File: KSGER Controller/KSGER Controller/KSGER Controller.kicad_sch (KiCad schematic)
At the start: 49 parts

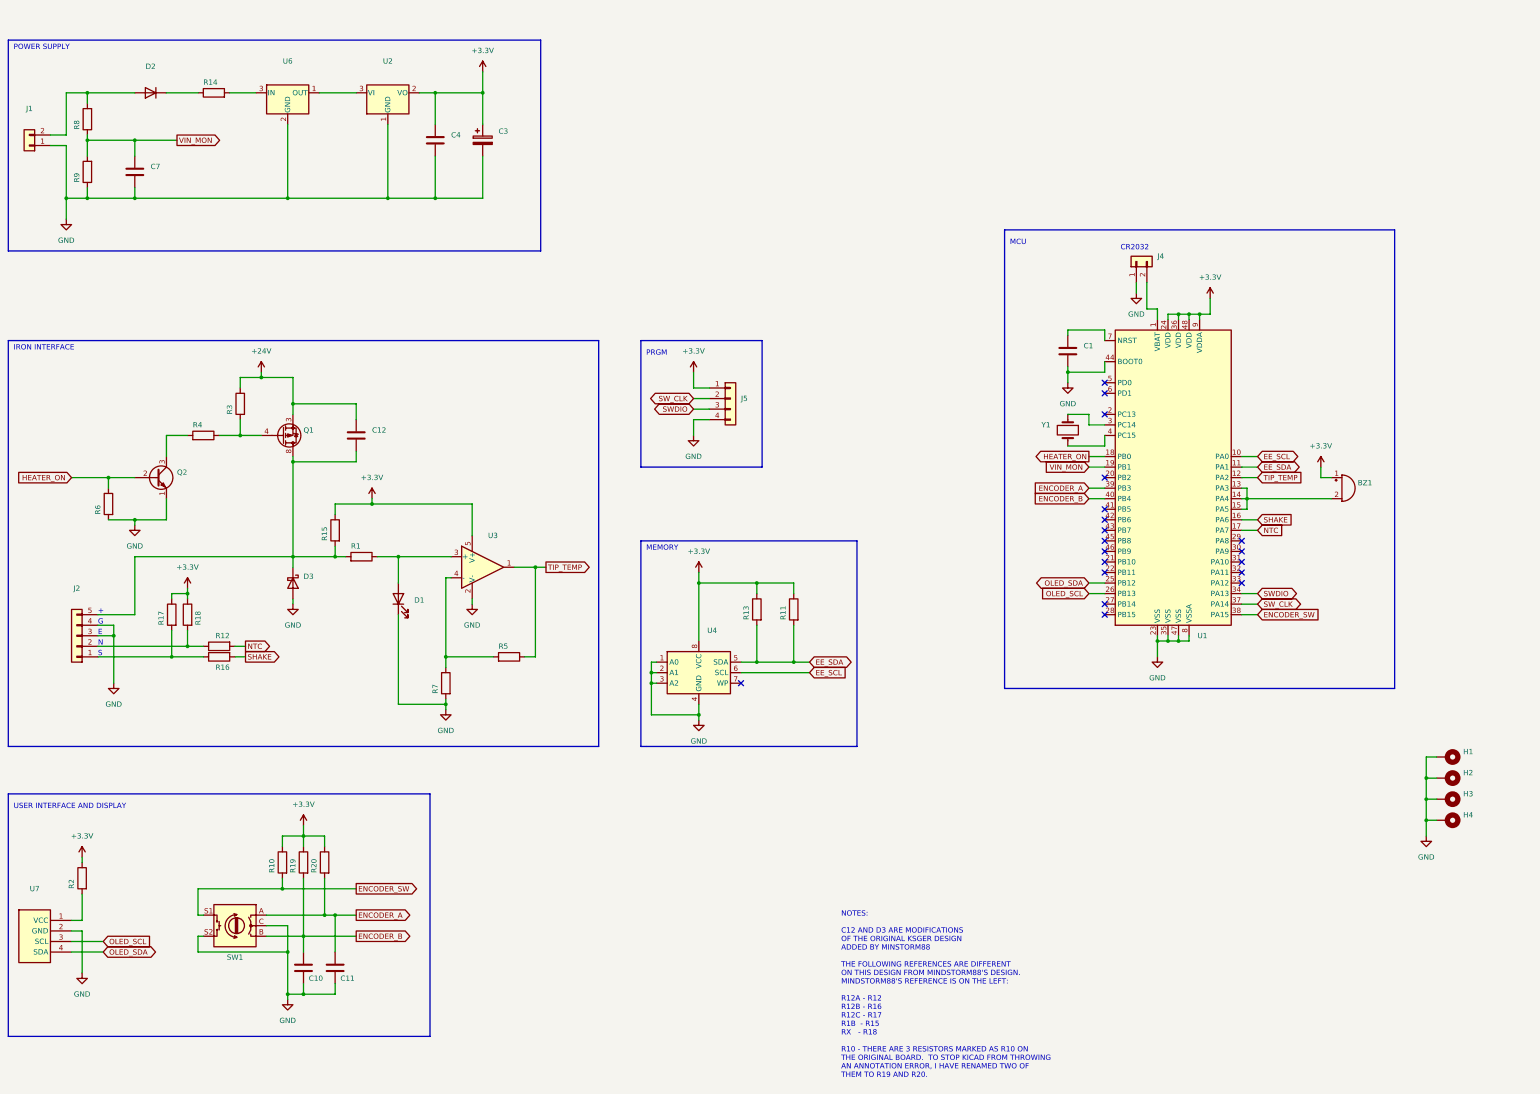
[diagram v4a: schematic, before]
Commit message: Added C5 and C6 from flobbydusts schematic
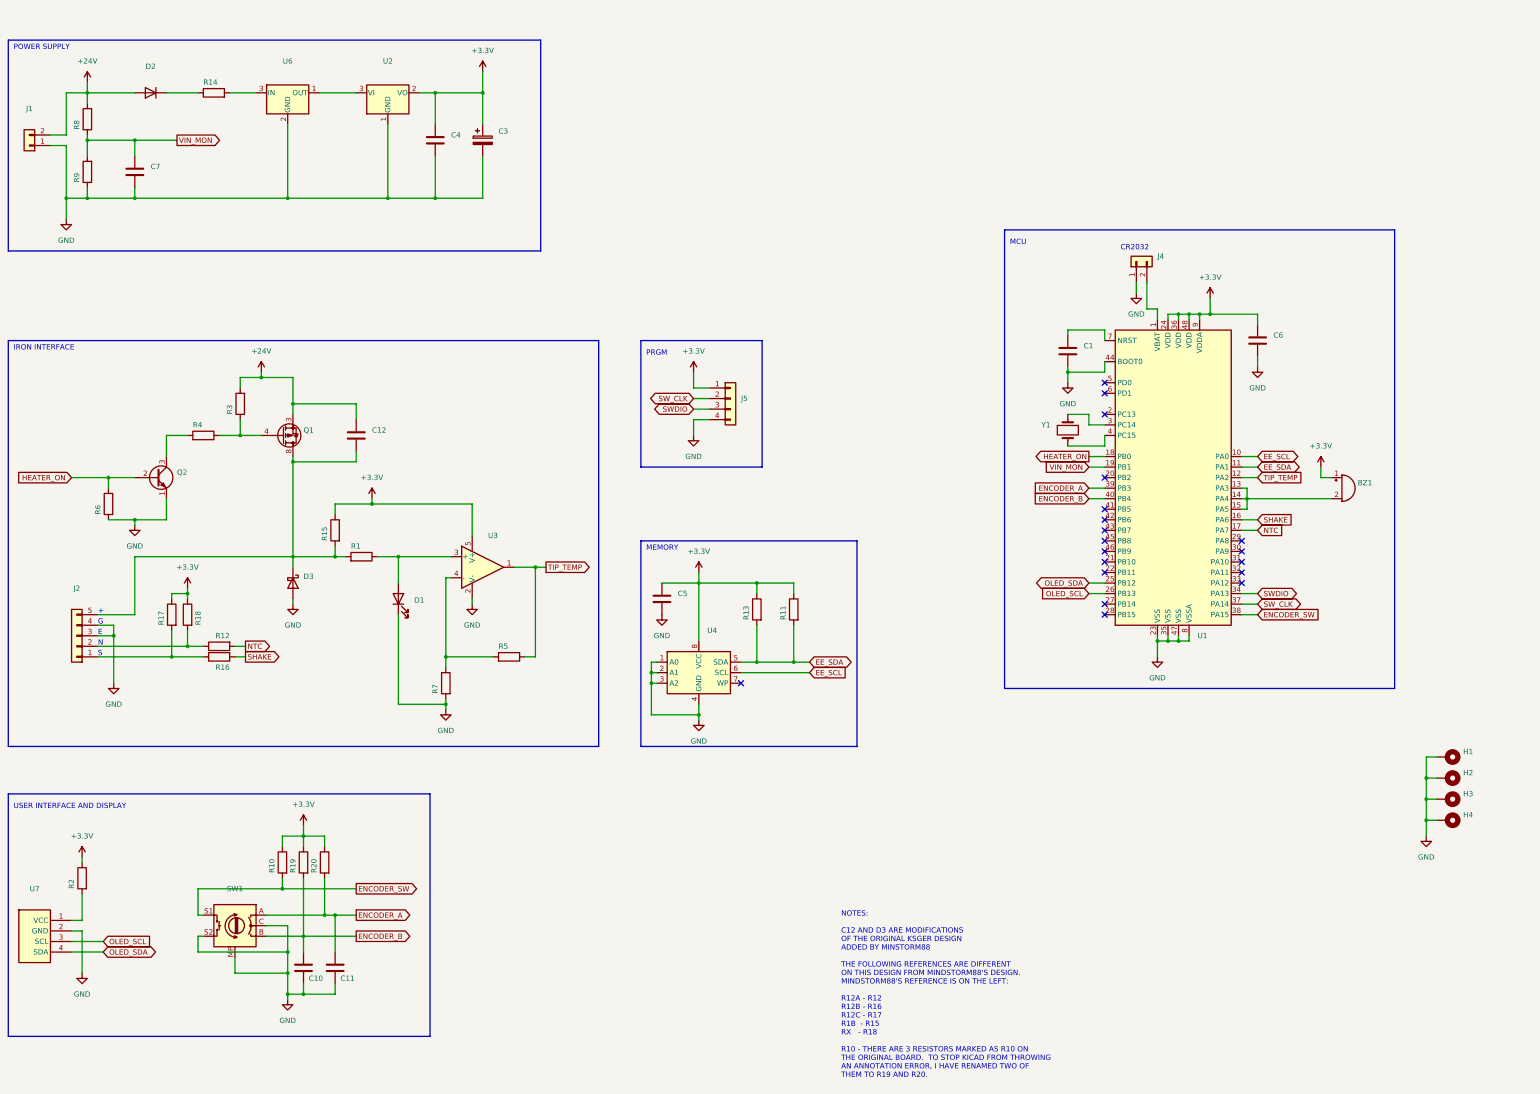
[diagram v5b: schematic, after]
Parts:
- added C5, C6: (no value), symbol Device:C
- SW1: symbol Device:RotaryEncoder_Switch -> KSGER Controller Parts:RotaryEncoder_Switch
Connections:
- net +24V: now also D2.2 (A), J1.2 (Pin_2), R8.2
- net +3V3: now also C5.1, C6.1
- net GND: now also SW1.MP, C5.2, C6.2
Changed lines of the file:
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@@
   (junction (at 76.2 175.26) (diameter 0) (color 0 0 0 0)
+  )
+  (junction (at 100.33 254) (diameter 0) (color 0 0 0 0)
+  )
+  (junction (at 322.58 95.25) (diameter 0) (color 0 0 0 0)
   )
   (junction (at 199.39 160.02) (diameter 0) (color 0 0 0 0)
@@
     (stroke (width 0) (type default) (color 0 0 0 0))
   )
+  (wire (pts (xy 190.5 160.02) (xy 199.39 160.02))
+    (stroke (width 0) (type default) (color 0 0 0 0))
+  )
   (wire (pts (xy 57.15 144.78) (xy 63.5 144.78))
     (stroke (width 0) (type default) (color 0 0 0 0))
@@
     (stroke (width 0) (type default) (color 0 0 0 0))
   )
+  (wire (pts (xy 100.33 254) (xy 100.33 259.08))
+    (stroke (width 0) (type default) (color 0 0 0 0))
+  )
   (wire (pts (xy 54.61 177.8) (xy 72.39 177.8))
     (stroke (width 0) (type default) (color 0 0 0 0))
@@
     (stroke (width 0) (type default) (color 0 0 0 0))
   )
+  (wire (pts (xy 87.63 250.19) (xy 87.63 254))
+    (stroke (width 0) (type default) (color 0 0 0 0))
+  )
+  (wire (pts (xy 334.01 95.25) (xy 322.58 95.25))
+    (stroke (width 0) (type default) (color 0 0 0 0))
+  )
   (wire (pts (xy 100.33 242.57) (xy 100.33 248.92))
     (stroke (width 0) (type default) (color 0 0 0 0))
@@
     (stroke (width 0) (type default) (color 0 0 0 0))
   )
+  (wire (pts (xy 52.07 39.37) (xy 52.07 41.91))
+    (stroke (width 0) (type default) (color 0 0 0 0))
+  )
   (wire (pts (xy 147.32 57.15) (xy 147.32 67.31))
     (stroke (width 0) (type default) (color 0 0 0 0))
@@
     (stroke (width 0) (type default) (color 0 0 0 0))
   )
+  (wire (pts (xy 334.01 97.79) (xy 334.01 95.25))
+    (stroke (width 0) (type default) (color 0 0 0 0))
+  )
   (wire (pts (xy 334.01 144.78) (xy 330.2 144.78))
     (stroke (width 0) (type default) (color 0 0 0 0))
@@
     (stroke (width 0) (type default) (color 0 0 0 0))
   )
+  (wire (pts (xy 334.01 107.95) (xy 334.01 105.41))
+    (stroke (width 0) (type default) (color 0 0 0 0))
+  )
   (wire (pts (xy 101.6 153.67) (xy 111.76 153.67))
     (stroke (width 0) (type default) (color 0 0 0 0))
@@
     (stroke (width 0) (type default) (color 0 0 0 0))
   )
-  (wire (pts (xy 100.33 248.92) (xy 100.33 259.08))
+  (wire (pts (xy 100.33 248.92) (xy 100.33 254))
+    (stroke (width 0) (type default) (color 0 0 0 0))
+  )
+  (wire (pts (xy 87.63 254) (xy 100.33 254))
     (stroke (width 0) (type default) (color 0 0 0 0))
   )
@@
     (pin "2")
   )
+  (symbol (lib_id "Device:C") (at 334.01 101.6 0) (unit 1)
+    (in_bom yes) (on_board yes) (fields_autoplaced)
+    (property "Reference" "C6" (id 0) (at 337.82 100.3299 0)
+      (effects (font (size 1.27 1.27)) (justify left))
+    )
+    (property "Value" "" (id 1) (at 337.82 102.8699 0)
+      (effects (font (size 1.27 1.27)) (justify left))
+    )
+    (property "Footprint" "" (id 2) (at 334.9752 105.41 0)
+      (effects (font (size 1.27 1.27)) hide)
+    )
+    (property "Datasheet" "~" (id 3) (at 334.01 101.6 0)
+      (effects (font (size 1.27 1.27)) hide)
+    )
+    (property "JCLPCB Part #" "C49678" (id 4) (at 334.01 101.6 0)
+      (effects (font (size 1.27 1.27)) hide)
+    )
+    (pin "1")
+    (pin "2")
+  )
   (symbol (lib_id "Device:R") (at 138.43 184.15 0) (mirror y) (unit 1)
     (in_bom yes) (on_board yes)
@@
     (pin "2")
   )
+  (symbol (lib_id "power:GND") (at 190.5 167.64 0) (unit 1)
+    (in_bom yes) (on_board yes) (fields_autoplaced)
+    (property "Reference" "#PWR?" (id 0) (at 190.5 173.99 0)
+      (effects (font (size 1.27 1.27)) hide)
+    )
+    (property "Value" "GND" (id 1) (at 190.5 172.72 0))
+    (property "Footprint" "" (id 2) (at 190.5 167.64 0)
+      (effects (font (size 1.27 1.27)) hide)
+    )
+    (property "Datasheet" "" (id 3) (at 190.5 167.64 0)
+      (effects (font (size 1.27 1.27)) hide)
+    )
+    (pin "1")
+  )
   (symbol (lib_id "Connector_Generic:Conn_01x05") (at 49.53 172.72 180) (unit 1)
     (in_bom yes) (on_board yes) (fields_autoplaced)
@@
     (pin "5")
   )
+  (symbol (lib_id "Device:C") (at 190.5 163.83 0) (unit 1)
+    (in_bom yes) (on_board yes) (fields_autoplaced)
+    (property "Reference" "C5" (id 0) (at 194.31 162.5599 0)
+      (effects (font (size 1.27 1.27)) (justify left))
+    )
+    (property "Value" "" (id 1) (at 194.31 165.0999 0)
+      (effects (font (size 1.27 1.27)) (justify left))
+    )
+    (property "Footprint" "" (id 2) (at 191.4652 167.64 0)
+      (effects (font (size 1.27 1.27)) hide)
+    )
+    (property "Datasheet" "~" (id 3) (at 190.5 163.83 0)
+      (effects (font (size 1.27 1.27)) hide)
+    )
+    (property "JCLPCB Part #" "C49678" (id 4) (at 190.5 163.83 0)
+      (effects (font (size 1.27 1.27)) hide)
+    )
+    (pin "1")
+    (pin "2")
+  )
   (symbol (lib_id "Device:R") (at 83.82 177.8 90) (mirror x) (unit 1)
     (in_bom yes) (on_board yes)
@@
     (pin "1")
     (pin "2")
+  )
+  (symbol (lib_id "power:GND") (at 334.01 107.95 0) (unit 1)
+    (in_bom yes) (on_board yes) (fields_autoplaced)
+    (property "Reference" "#PWR?" (id 0) (at 334.01 114.3 0)
+      (effects (font (size 1.27 1.27)) hide)
+    )
+    (property "Value" "GND" (id 1) (at 334.01 113.03 0))
+    (property "Footprint" "" (id 2) (at 334.01 107.95 0)
+      (effects (font (size 1.27 1.27)) hide)
+    )
+    (property "Datasheet" "" (id 3) (at 334.01 107.95 0)
+      (effects (font (size 1.27 1.27)) hide)
+    )
+    (pin "1")
   )
   (symbol (lib_id "power:+3.3V") (at 104.14 218.44 0) (unit 1)
@@
     (pin "2")
   )
+  (symbol (lib_id "power:+24V") (at 52.07 39.37 0) (unit 1)
+    (in_bom yes) (on_board yes) (fields_autoplaced)
+    (property "Reference" "#PWR0124" (id 0) (at 52.07 43.18 0)
+      (effects (font (size 1.27 1.27)) hide)
+    )
+    (property "Value" "+24V" (id 1) (at 52.07 34.29 0))
+    (property "Footprint" "" (id 2) (at 52.07 39.37 0)
+      (effects (font (size 1.27 1.27)) hide)
+    )
+    (property "Datasheet" "" (id 3) (at 52.07 39.37 0)
+      (effects (font (size 1.27 1.27)) hide)
+    )
+    (pin "1")
+  )
   (symbol (lib_id "Mechanical:MountingHole_Pad") (at 379.73 217.17 270) (unit 1)
     (in_bom yes) (on_board yes) (fields_autoplaced)
@@
     (pin "1")
   )
-  (symbol (lib_id "Device:RotaryEncoder_Switch") (at 87.63 242.57 0) (mirror y) (unit 1)
+  (symbol (lib_id "KSGER Controller Parts:RotaryEncoder_Switch") (at 87.63 242.57 0) (mirror y) (unit 1)
     (in_bom yes) (on_board yes)
-    (property "Reference" "SW1" (id 0) (at 87.63 250.19 0))
-    (property "Value" "" (id 1) (at 87.63 252.73 0))
+    (property "Reference" "SW1" (id 0) (at 87.63 233.68 0))
+    (property "Value" "" (id 1) (at 87.63 236.22 0))
     (property "Footprint" "" (id 2) (at 91.44 238.506 0)
       (effects (font (size 1.27 1.27)) hide)
@@
     (pin "B")
     (pin "C")
+    (pin "MP")
     (pin "S1")
     (pin "S2")
@@
       (reference "#PWR0123") (unit 1) (value "+3.3V") (footprint "")
     )
+    (path "/ed517164-08ae-478b-8a98-824a9a4f4302"
+      (reference "#PWR0124") (unit 1) (value "+24V") (footprint "")
+    )
+    (path "/4be60d7b-8464-457c-9bcb-a7b7d28f700b"
+      (reference "#PWR?") (unit 1) (value "GND") (footprint "")
+    )
+    (path "/65f47267-2094-4ab7-b13a-078a72b97974"
+      (reference "#PWR?") (unit 1) (value "GND") (footprint "")
+    )
     (path "/6430ee94-0845-46e9-b4c5-a76fd904b861"
       (reference "BZ1") (unit 1) (value "Buzzer") (footprint "Connector_JST:JST_EH_B2B-EH-A_1x02_P2.50mm_Vertical")
@@
       (reference "C4") (unit 1) (value "0.1") (footprint "Capacitor_SMD:C_0805_2012Metric")
     )
+    (path "/4fd90282-64df-4046-974c-926d6049077a"
+      (reference "C5") (unit 1) (value "0.1") (footprint "Capacitor_SMD:C_0805_2012Metric")
+    )
+    (path "/384f01f2-7874-478d-8f4b-b16b98237a62"
+      (reference "C6") (unit 1) (value "0.1") (footprint "Capacitor_SMD:C_0805_2012Metric")
+    )
     (path "/0dee4f6e-be04-448a-8b0a-20d1b7912c60"

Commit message: Added PWR_FLAGs to resolve some ERC errors
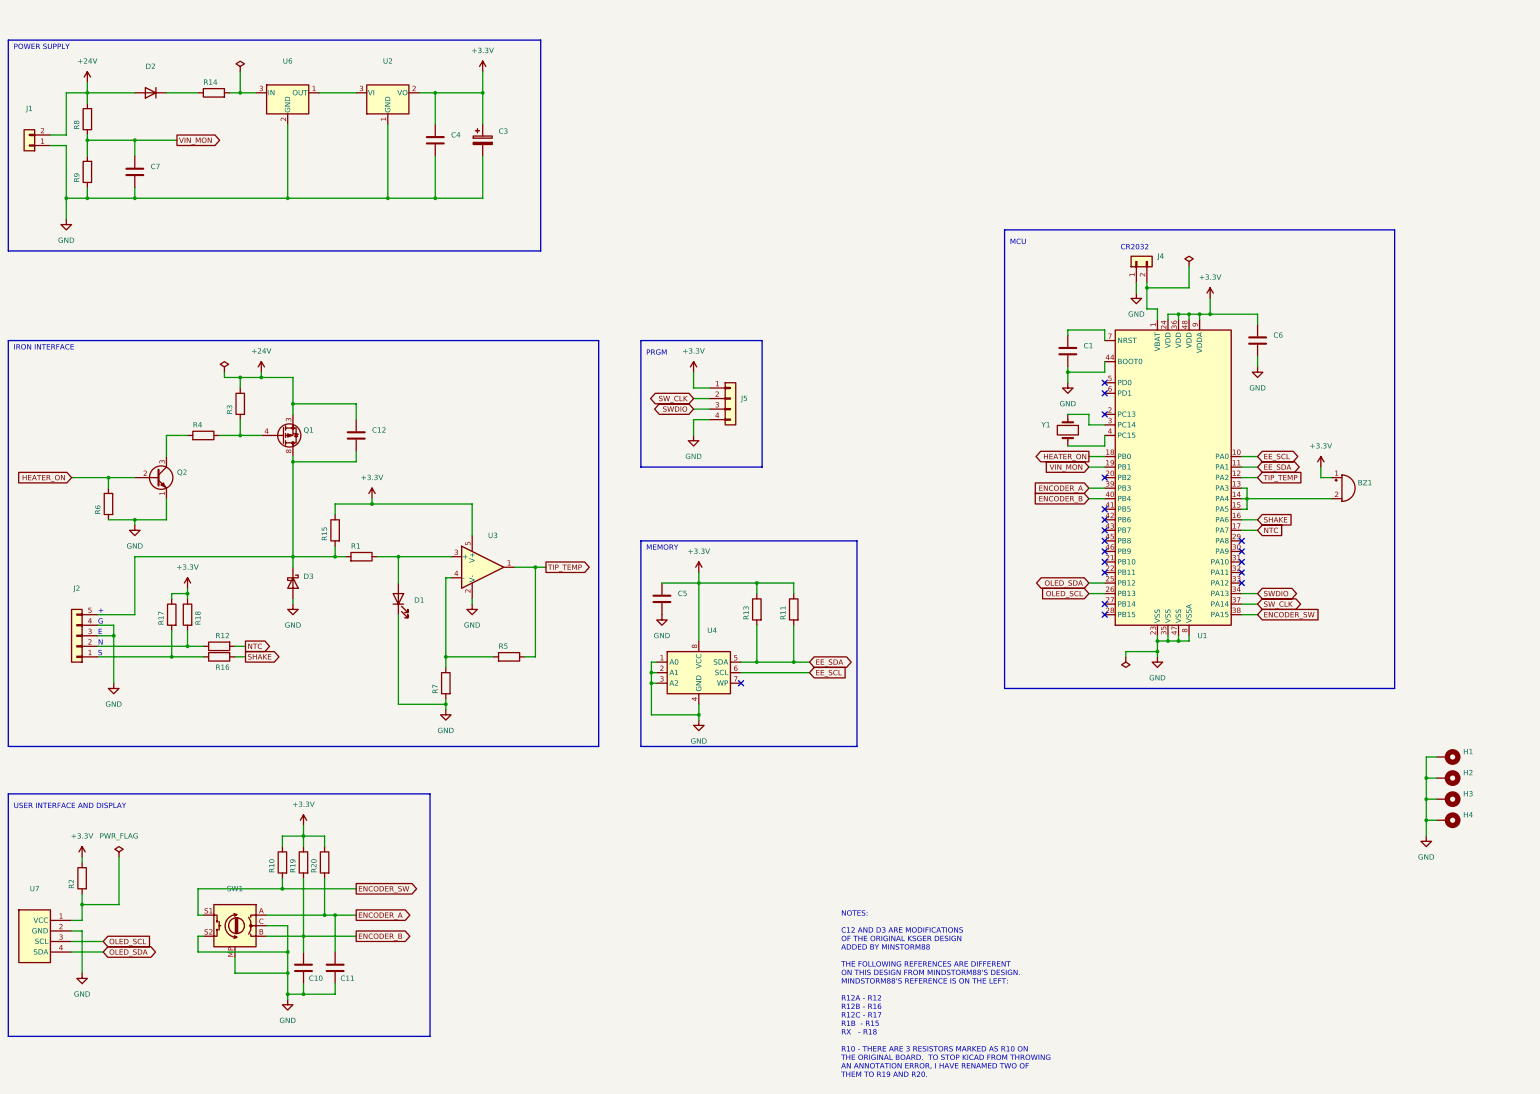
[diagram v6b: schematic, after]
